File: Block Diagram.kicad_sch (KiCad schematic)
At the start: 39 parts, among them J1001 Header, J701 ZHOURI DC3, J800 Molex 430451227, J901 Header

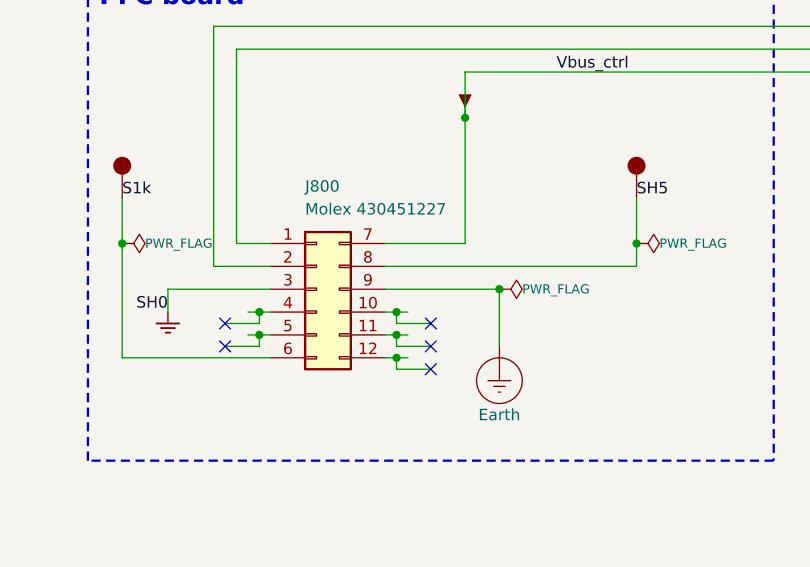
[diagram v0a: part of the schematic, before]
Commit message: Placement started
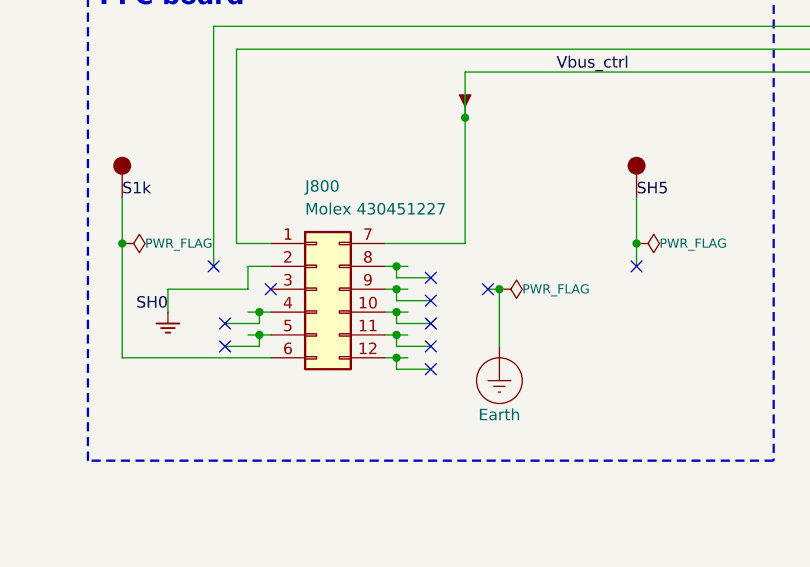
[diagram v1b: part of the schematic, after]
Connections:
- net Earth: no longer J800.9 (Pin_9)
- net MCU/SUP_TX: no longer J800.2 (Pin_2)
- net SH0: now also J800.2 (Pin_2); no longer J800.3 (Pin_3)
- net SH5: no longer J800.8 (Pin_8)
- no-connect marks 5 -> 11
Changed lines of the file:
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@@
+	)
+	(junction
+		(at 130.81 180.34)
+		(diameter 0)
+		(color 0 0 0 0)
+	)
+	(junction
+		(at 161.29 182.88)
+		(diameter 0)
+		(color 0 0 0 0)
+	)
+	(junction
+		(at 161.29 185.42)
+		(diameter 0)
+		(color 0 0 0 0)
+	)
+	(junction
+		(at 146.05 187.96)
+		(diameter 0)
+		(color 0 0 0 0)
 	)
 	(junction
@@
 	)
 	(junction
-		(at 130.81 180.34)
-		(diameter 0)
-		(color 0 0 0 0)
-	)
-	(junction
-		(at 146.05 187.96)
-		(diameter 0)
-		(color 0 0 0 0)
-	)
-	(junction
 		(at 334.01 144.78)
 		(diameter 0)
@@
 	)
 	(no_connect
+		(at 165.1 186.69)
+	)
+	(no_connect
 		(at 142.24 191.77)
+	)
+	(no_connect
+		(at 140.97 182.88)
+	)
+	(no_connect
+		(at 187.96 182.88)
+	)
+	(no_connect
+		(at 171.45 185.42)
 	)
 	(no_connect
@@
 	)
 	(no_connect
+		(at 147.32 185.42)
+	)
+	(no_connect
 		(at 142.24 189.23)
+	)
+	(no_connect
+		(at 165.1 184.15)
 	)
 	(no_connect
@@
 	(wire
 		(pts
+			(xy 144.78 182.88) (xy 144.78 185.42)
+		)
+		(stroke
+			(width 0)
+			(type default)
+		)
+	)
+	(wire
+		(pts
 			(xy 111.76 92.71) (xy 111.76 91.44)
 		)
@@
 	(wire
 		(pts
+			(xy 162.56 185.42) (xy 161.29 185.42)
+		)
+		(stroke
+			(width 0)
+			(type default)
+		)
+	)
+	(wire
+		(pts
 			(xy 168.91 161.29) (xy 215.9 161.29)
 		)
@@
 	(wire
 		(pts
-			(xy 160.02 185.42) (xy 172.72 185.42)
-		)
-		(stroke
-			(width 0)
-			(type default)
-		)
-	)
-	(wire
-		(pts
 			(xy 361.95 127) (xy 359.41 127)
 		)
@@
 	(wire
 		(pts
+			(xy 161.29 185.42) (xy 160.02 185.42)
+		)
+		(stroke
+			(width 0)
+			(type default)
+		)
+	)
+	(wire
+		(pts
 			(xy 187.96 180.34) (xy 187.96 182.88)
 		)
@@
 	(wire
 		(pts
+			(xy 161.29 182.88) (xy 160.02 182.88)
+		)
+		(stroke
+			(width 0)
+			(type default)
+		)
+	)
+	(wire
+		(pts
 			(xy 146.05 187.96) (xy 147.32 187.96)
 		)
@@
 	(wire
 		(pts
-			(xy 135.89 185.42) (xy 147.32 185.42)
+			(xy 135.89 185.42) (xy 144.78 185.42)
 		)
 		(stroke
@@
 	(wire
 		(pts
-			(xy 147.32 182.88) (xy 140.97 182.88)
-		)
-		(stroke
-			(width 0)
-			(type default)
-		)
-	)
-	(wire
-		(pts
 			(xy 339.09 127) (xy 339.09 129.54)
 		)
@@
 	(wire
 		(pts
+			(xy 165.1 184.15) (xy 161.29 184.15)
+		)
+		(stroke
+			(width 0)
+			(type default)
+		)
+	)
+	(wire
+		(pts
 			(xy 336.55 129.54) (xy 336.55 127)
 		)
@@
 	(wire
 		(pts
+			(xy 161.29 185.42) (xy 161.29 186.69)
+		)
+		(stroke
+			(width 0)
+			(type default)
+		)
+	)
+	(wire
+		(pts
 			(xy 304.8 144.78) (xy 328.93 144.78)
 		)
@@
 	(wire
 		(pts
+			(xy 162.56 182.88) (xy 161.29 182.88)
+		)
+		(stroke
+			(width 0)
+			(type default)
+		)
+	)
+	(wire
+		(pts
+			(xy 171.45 185.42) (xy 172.72 185.42)
+		)
+		(stroke
+			(width 0)
+			(type default)
+		)
+	)
+	(wire
+		(pts
 			(xy 161.29 190.5) (xy 161.29 191.77)
 		)
@@
 	(wire
 		(pts
-			(xy 160.02 182.88) (xy 187.96 182.88)
-		)
-		(stroke
-			(width 0)
-			(type default)
-		)
-	)
-	(wire
-		(pts
 			(xy 203.2 113.03) (xy 215.9 113.03)
 		)
@@
 	(wire
 		(pts
+			(xy 165.1 186.69) (xy 161.29 186.69)
+		)
+		(stroke
+			(width 0)
+			(type default)
+		)
+	)
+	(wire
+		(pts
 			(xy 142.24 191.77) (xy 146.05 191.77)
 		)
@@
 	(wire
 		(pts
+			(xy 161.29 182.88) (xy 161.29 184.15)
+		)
+		(stroke
+			(width 0)
+			(type default)
+		)
+	)
+	(wire
+		(pts
 			(xy 213.36 92.71) (xy 213.36 91.44)
 		)
@@
 		(pts
 			(xy 187.96 175.26) (xy 187.96 180.34)
+		)
+		(stroke
+			(width 0)
+			(type default)
+		)
+	)
+	(wire
+		(pts
+			(xy 147.32 182.88) (xy 144.78 182.88)
 		)
 		(stroke
@@
 		(length 2.54)
 		(shape dot)
+		(at 162.56 185.42 270)
+		(effects
+			(font
+				(size 1.27 1.27)
+			)
+			(justify right bottom)
+		)
+		(property "Netclass" "NR"
+			(at 165.735 185.42 0)
+			(effects
+				(font
+					(size 1.016 1.016)
+				)
+				(justify left)
+			)
+		)
+		(property "Component Class" ""
+			(at -175.26 105.41 0)
+			(effects
+				(font
+					(size 1.27 1.27)
+					(italic yes)
+				)
+				(justify right)
+			)
+		)
+	)
+	(netclass_flag ""
+		(length 2.54)
+		(shape dot)
 		(at 162.56 190.5 270)
 		(effects
@@
 			(effects
 				(font
+					(size 1.27 1.27)
+					(italic yes)
+				)
+				(justify right)
+			)
+		)
+	)
+	(netclass_flag ""
+		(length 2.54)
+		(shape dot)
+		(at 162.56 182.88 270)
+		(effects
+			(font
+				(size 1.27 1.27)
+			)
+			(justify right bottom)
+		)
+		(property "Netclass" "NR"
+			(at 165.735 182.88 0)
+			(effects
+				(font
+					(size 1.016 1.016)
+				)
+				(justify left)
+			)
+		)
+		(property "Component Class" ""
+			(at -175.26 102.87 0)
+			(effects
+				(font

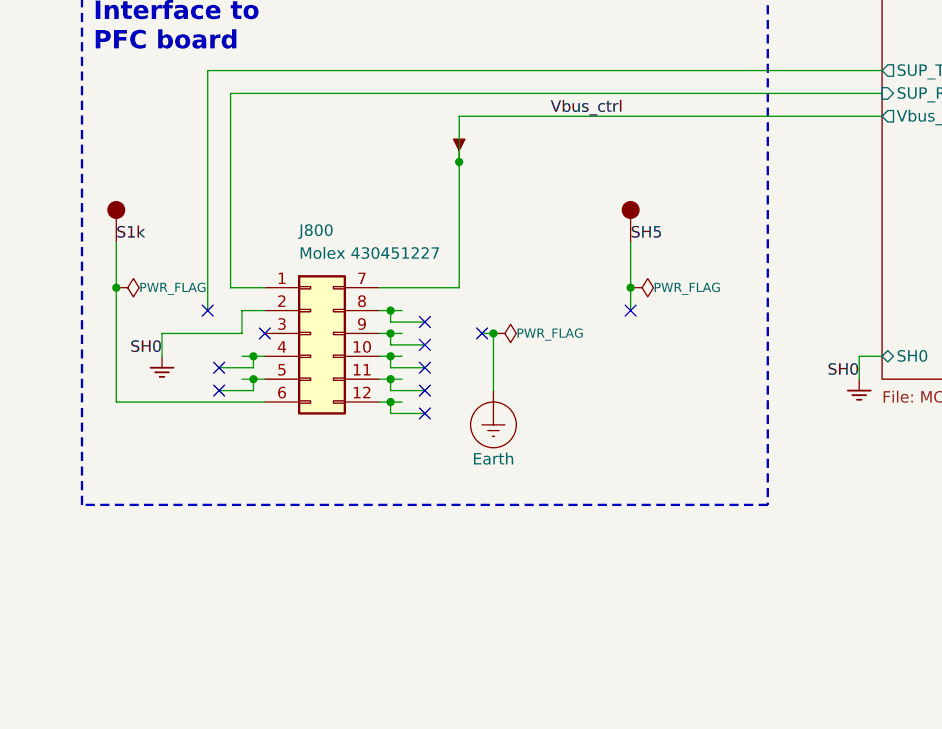
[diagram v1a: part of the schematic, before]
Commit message: New placement strategy
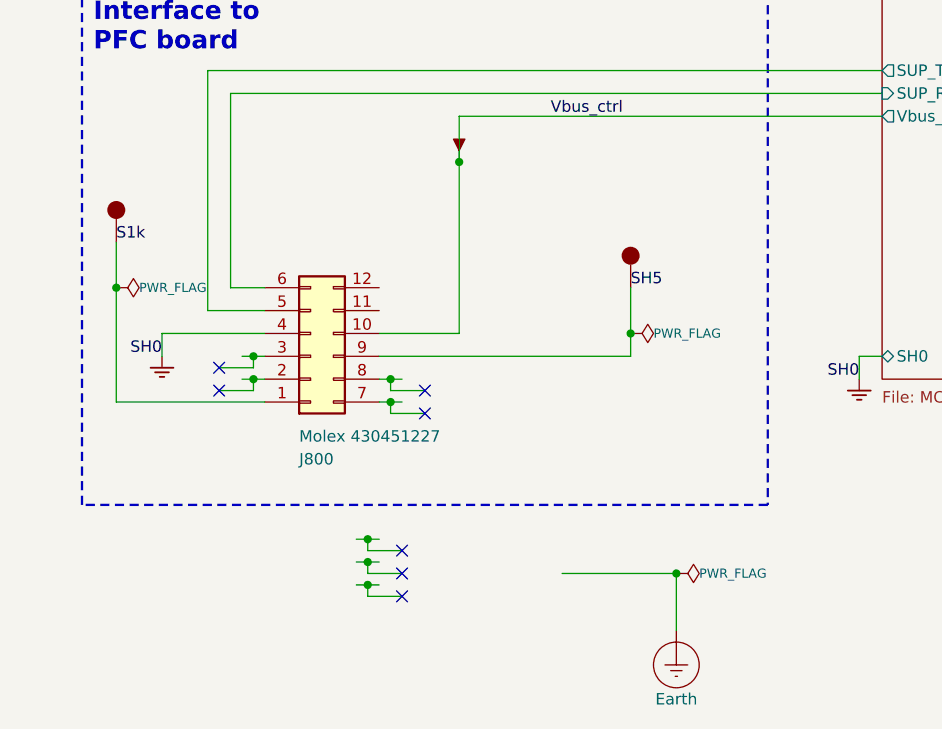
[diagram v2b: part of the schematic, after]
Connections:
- net MCU/SUP_RX: now also J800.6 (Pin_6); no longer J800.1 (Pin_1)
- net MCU/SUP_TX: now also J800.5 (Pin_5)
- net S1k: now also J800.1 (Pin_1); no longer J800.6 (Pin_6)
- net SH0: now also J800.4 (Pin_4); no longer J800.2 (Pin_2)
- net SH5: now also J800.9 (Pin_9)
- net Vbus_ctrl: now also J800.10 (Pin_10); no longer J800.7 (Pin_7)
- no-connect marks 11 -> 7

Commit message: TP placement candidate 90%
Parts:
- removed R701, R702: 0R, Resistor_SMD:R_1206_3216Metric_Pad1.30x1.75mm_HandSolder, symbol Device:R
- added H100: MountingHole_Pad, MountingHole:MountingHole_3.2mm_M3_DIN965_Pad_TopBottom, symbol Mechanical:MountingHole_Pad
- added P139: ~, symbol personal:Cosmetic_GND
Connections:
- net Earth: now also J701.2 (Pin_2), J701.4 (Pin_4), H100.1
- net S1k: now also J800.7 (Pin_7); no longer J800.1 (Pin_1)
- net SH0: now also J800.10 (Pin_10), P139.1
- net SH5: now also J800.11 (Pin_11); no longer J800.9 (Pin_9)
- net Vbus_ctrl: now also J800.12 (Pin_12); no longer J800.10 (Pin_10)
- no-connect marks 7 -> 6

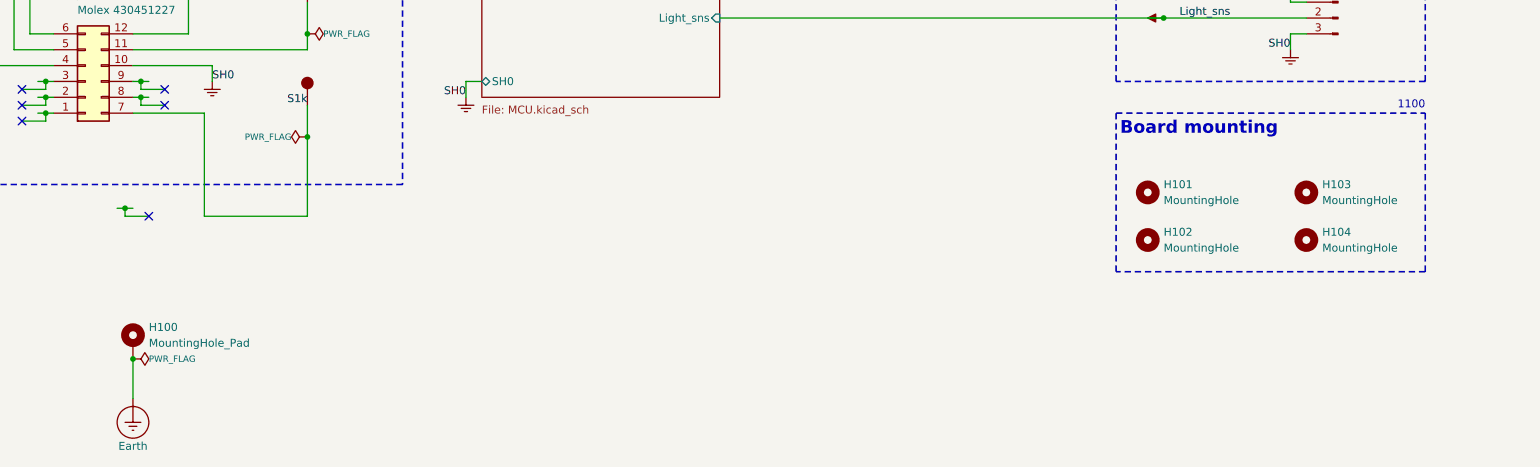
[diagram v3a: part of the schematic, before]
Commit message: Placement complplete, feasibility routing complete
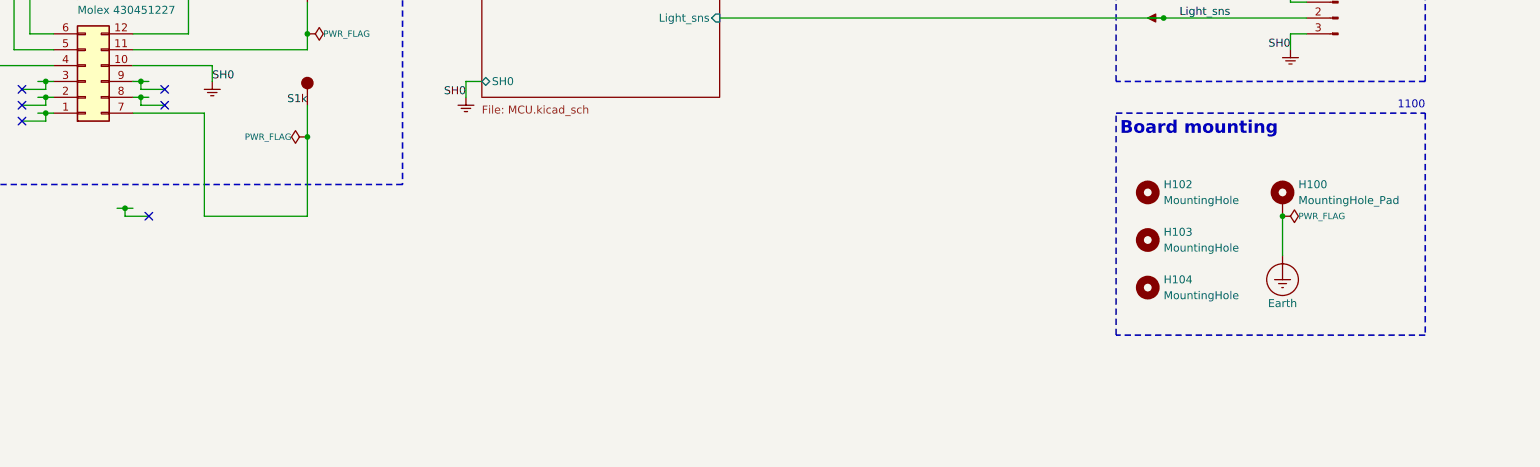
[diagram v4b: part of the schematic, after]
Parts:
- removed H101: MountingHole, MountingHole:MountingHole_3.2mm_M3, symbol Mechanical:MountingHole
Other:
- moved on the sheet: H100, H102, H103, H104
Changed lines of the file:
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@@
 	(rectangle
 		(start 317.5 193.04)
-		(end 367.03 218.44)
+		(end 367.03 228.6)
 		(stroke
 			(width 0.254)
@@
 	)
 	(junction
-		(at 160.02 232.41)
+		(at 344.17 209.55)
 		(diameter 0)
 		(color 0 0 0 0)
@@
 	(wire
 		(pts
-			(xy 160.02 238.76) (xy 160.02 232.41)
+			(xy 344.17 215.9) (xy 344.17 209.55)
 		)
 		(stroke
@@
 		(length 2.54)
 		(shape dot)
-		(at 160.02 237.49 270)
+		(at 344.17 214.63 270)
 		(effects
 			(font
@@
 		)
 		(property "Netclass" "LV"
-			(at 165.1 237.49 0)
+			(at 349.25 214.63 0)
 			(effects
 				(font
@@
 		)
 		(property "Component Class" ""
-			(at 387.35 191.77 0)
+			(at 571.5 168.91 0)
 			(effects
 				(font
@@
 	(symbol
 		(lib_id "Mechanical:MountingHole")
-		(at 322.58 213.36 0)
+		(at 322.58 205.74 0)
 		(unit 1)
 		(exclude_from_sim no)
@@
 		(fields_autoplaced yes)
 		(property "Reference" "H102"
-			(at 325.12 212.0899 0)
+			(at 325.12 204.4699 0)
 			(effects
 				(font
@@
 		)
 		(property "Value" "MountingHole"
-			(at 325.12 214.6299 0)
+			(at 325.12 207.0099 0)
 			(effects
 				(font
@@
 		)
 		(property "Footprint" "MountingHole:MountingHole_3.2mm_M3"
-			(at 322.58 213.36 0)
+			(at 322.58 205.74 0)
 			(effects
 				(font
@@
 		)
 		(property "Datasheet" "~"
-			(at 322.58 213.36 0)
+			(at 322.58 205.74 0)
 			(effects
 				(font
@@
 		)
 		(property "Description" "Mounting Hole without connection"
-			(at 322.58 213.36 0)
+			(at 322.58 205.74 0)
 			(effects
 				(font
@@
 		)
 		(property "Config" ""
-			(at 322.58 213.36 0)
+			(at 322.58 205.74 0)
 			(effects
 				(font
@@
 		)
 		(property "Manufacturer" ""
-			(at 322.58 213.36 0)
+			(at 322.58 205.74 0)
 			(effects
 				(font
@@
 		)
 		(property "Manufacturer Part Number" ""
-			(at 322.58 213.36 0)
+			(at 322.58 205.74 0)
 			(effects
 				(font
@@
 	(symbol
 		(lib_id "power:PWR_FLAG")
-		(at 160.02 232.41 270)
+		(at 344.17 209.55 270)
 		(unit 1)
 		(exclude_from_sim no)
@@
 		(dnp no)
 		(property "Reference" "#FLG05"
-			(at 161.925 232.41 0)
+			(at 346.075 209.55 0)
 			(effects
 				(font
@@
 		)
 		(property "Value" "PWR_FLAG"
-			(at 162.56 232.41 90)
+			(at 346.71 209.55 90)
 			(effects
 				(font
@@
 		)
 		(property "Footprint" ""
-			(at 160.02 232.41 0)
+			(at 344.17 209.55 0)
 			(effects
 				(font
@@
 		)
 		(property "Datasheet" "~"
-			(at 160.02 232.41 0)
+			(at 344.17 209.55 0)
 			(effects
 				(font
@@
 		)
 		(property "Description" "Special symbol for telling ERC where power comes from"
-			(at 160.02 232.41 0)
+			(at 344.17 209.55 0)
 			(effects
 				(font
@@
 	(symbol
 		(lib_id "Mechanical:MountingHole_Pad")
-		(at 160.02 229.87 0)
+		(at 344.17 207.01 0)
 		(unit 1)
 		(exclude_from_sim no)
@@
 		(fields_autoplaced yes)
 		(property "Reference" "H100"
-			(at 162.56 227.3299 0)
+			(at 346.71 204.4699 0)
 			(effects
 				(font
@@
 		)
 		(property "Value" "MountingHole_Pad"
-			(at 162.56 229.8699 0)
+			(at 346.71 207.0099 0)
 			(effects
 				(font
@@
 		)
 		(property "Footprint" "MountingHole:MountingHole_3.2mm_M3_DIN965_Pad_TopBottom"
-			(at 160.02 229.87 0)
+			(at 344.17 207.01 0)
 			(effects
 				(font
@@
 		)
 		(property "Datasheet" "~"
-			(at 160.02 229.87 0)
+			(at 344.17 207.01 0)
 			(effects
 				(font
@@
 		)
 		(property "Description" "Mounting Hole with connection"
-			(at 160.02 229.87 0)
+			(at 344.17 207.01 0)
 			(effects
 				(font
@@
 	(symbol
 		(lib_id "power:Earth_Protective")
-		(at 160.02 238.76 0)
+		(at 344.17 215.9 0)
 		(unit 1)
 		(exclude_from_sim no)
@@
 		(dnp no)
 		(property "Reference" "#PWR01"
-			(at 160.02 248.92 0)
+			(at 344.17 226.06 0)
 			(effects
 				(font
@@
 		)
 		(property "Value" "Earth"
-			(at 160.02 246.38 0)
+			(at 344.17 223.52 0)
 			(effects
 				(font
@@
 		)
 		(property "Footprint" ""
-			(at 160.02 241.3 0)
+			(at 344.17 218.44 0)
 			(effects
 				(font
@@
 		)
 		(property "Datasheet" "~"
-			(at 160.02 241.3 0)
+			(at 344.17 218.44 0)
 			(effects
 				(font
@@
 		)
 		(property "Description" "Power symbol creates a global label with name \"Earth_Protective\""
-			(at 160.02 238.76 0)
+			(at 344.17 215.9 0)
 			(effects
 				(font
@@
 	(symbol
 		(lib_id "Mechanical:MountingHole")
-		(at 347.98 213.36 0)
+		(at 322.58 220.98 0)
 		(unit 1)
 		(exclude_from_sim no)
@@
 		(fields_autoplaced yes)
 		(property "Reference" "H104"
-			(at 350.52 212.0899 0)
+			(at 325.12 219.7099 0)
 			(effects
 				(font
@@
 		)
 		(property "Value" "MountingHole"
-			(at 350.52 214.6299 0)
+			(at 325.12 222.2499 0)
 			(effects
 				(font
@@
 		)
 		(property "Footprint" "MountingHole:MountingHole_3.2mm_M3"
-			(at 347.98 213.36 0)
+			(at 322.58 220.98 0)
 			(effects
 				(font
@@
 		)
 		(property "Datasheet" "~"
-			(at 347.98 213.36 0)
+			(at 322.58 220.98 0)
 			(effects
 				(font
@@
 		)
 		(property "Description" "Mounting Hole without connection"
-			(at 347.98 213.36 0)
+			(at 322.58 220.98 0)
 			(effects
 				(font
@@
 		)
 		(property "Config" ""
-			(at 347.98 213.36 0)
+			(at 322.58 220.98 0)
 			(effects
 				(font
@@
 		)
 		(property "Manufacturer" ""
-			(at 347.98 213.36 0)
+			(at 322.58 220.98 0)
 			(effects
 				(font
@@
 		)
 		(property "Manufacturer Part Number" ""
-			(at 347.98 213.36 0)
+			(at 322.58 220.98 0)
 			(effects
 				(font
@@
 	)
 	(symbol
-		(lib_id "Mechanical:MountingHole")
-		(at 322.58 205.74 0)
-		(unit 1)
-		(exclude_from_sim no)
-		(in_bom no)
-		(on_board yes)
-		(dnp no)
-		(fields_autoplaced yes)
-		(property "Reference" "H101"
-			(at 325.12 204.4699 0)
-			(effects
-				(font
-					(size 1.27 1.27)
-				)
-				(justify left)
-			)
-		)
-		(property "Value" "MountingHole"
-			(at 325.12 207.0099 0)
-			(effects
-				(font
-					(size 1.27 1.27)
-				)
-				(justify left)
-			)
-		)
-		(property "Footprint" "MountingHole:MountingHole_3.2mm_M3"
-			(at 322.58 205.74 0)
-			(effects
-				(font
-					(size 1.27 1.27)
-				)
-				(hide yes)
-			)
-		)
-		(property "Datasheet" "~"
-			(at 322.58 205.74 0)
-			(effects
-				(font
-					(size 1.27 1.27)
-				)
-				(hide yes)
-			)
-		)
-		(property "Description" "Mounting Hole without connection"
-			(at 322.58 205.74 0)
-			(effects
-				(font
-					(size 1.27 1.27)
-				)
-				(hide yes)
-			)
-		)
-		(property "Config" ""
-			(at 322.58 205.74 0)
-			(effects
-				(font
-					(size 1.27 1.27)
-				)
-				(hide yes)
-			)
-		)
-		(property "Manufacturer" ""
-			(at 322.58 205.74 0)
-			(effects
-				(font
-					(size 1.27 1.27)
-				)
-				(hide yes)
-			)
-		)
-		(property "Manufacturer Part Number" ""
-			(at 322.58 205.74 0)
-			(effects
-				(font
-					(size 1.27 1.27)
-				)
-				(hide yes)
-			)
-		)
-		(instances
-			(project "Strobe_main"
-				(path "/f9e05184-c88b-4a88-ae9c-ab2bdb32be7c/82da9dbf-ba38-4d08-ba35-a220fa2963b1"
-					(reference "H101")
-					(unit 1)
-				)
-			)
-		)
-	)
-	(symbol
 		(lib_id "personal:Cosmetic_PWR")
 		(at 213.36 91.44 0)
@@
 	(symbol
 		(lib_id "Mechanical:MountingHole")
-		(at 347.98 205.74 0)
+		(at 322.58 213.36 0)
 		(unit 1)
 		(exclude_from_sim no)
@@
 		(fields_autoplaced yes)
 		(property "Reference" "H103"
-			(at 350.52 204.4699 0)
+			(at 325.12 212.0899 0)
 			(effects
 				(font
@@
 		)
 		(property "Value" "MountingHole"
-			(at 350.52 207.0099 0)
+			(at 325.12 214.6299 0)
 			(effects
 				(font
@@
 		)
 		(property "Footprint" "MountingHole:MountingHole_3.2mm_M3"
-			(at 347.98 205.74 0)
+			(at 322.58 213.36 0)
 			(effects
 				(font
@@
 		)
 		(property "Datasheet" "~"
-			(at 347.98 205.74 0)
+			(at 322.58 213.36 0)
 			(effects
 				(font
@@
 		)
 		(property "Description" "Mounting Hole without connection"
-			(at 347.98 205.74 0)
+			(at 322.58 213.36 0)
 			(effects
 				(font
@@
 		)
 		(property "Config" ""
-			(at 347.98 205.74 0)
+			(at 322.58 213.36 0)
 			(effects
 				(font
@@
 		)
 		(property "Manufacturer" ""
-			(at 347.98 205.74 0)
+			(at 322.58 213.36 0)
 			(effects
 				(font
@@
 		)
 		(property "Manufacturer Part Number" ""
-			(at 347.98 205.74 0)
+			(at 322.58 213.36 0)
 			(effects
 				(font
